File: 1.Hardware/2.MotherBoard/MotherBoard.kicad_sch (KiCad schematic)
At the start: 48 parts, among them J1 PWR, J2 MOTOR, SW1 SW_SPDT, U1 SCEP_CH32V3, U2 RT9013-33GB

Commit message: MotherBoard sch
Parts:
- added BZ1: Buzzer, ErBW_s:Buzzer_9*9P5, symbol Device:Buzzer
- added D7: 1N4148W, Diode_SMD:D_SMA, symbol Diode:1N4148W
- added J3: SWD, symbol Connector_Generic:Conn_02x04_Odd_Even
- added J4: WIRELESS, Connector_PinHeader_2.54mm:PinHeader_1x04_P2.54mm_Vertical, symbol Connector_Generic:Conn_01x04
- added J5: FLY_WHEEL, Connector_PinHeader_2.54mm:PinHeader_2x03_P2.54mm_Vertical, symbol Connector_Generic:Conn_02x03_Odd_Even
- added J6: MOTOR_BACK, Connector_PinHeader_2.54mm:PinHeader_2x03_P2.54mm_Vertical, symbol Connector_Generic:Conn_02x03_Odd_Even
- added J7: SERVO, Connector_PinHeader_2.54mm:PinHeader_1x03_P2.54mm_Vertical, symbol Connector_Generic:Conn_01x03
- added J8: MOTOR, ErBW_s:VCC_CONN, symbol Connector_Generic:Conn_01x02
- added J9: 9-Axis, Connector_PinHeader_2.54mm:PinHeader_1x04_P2.54mm_Vertical, symbol Connector_Generic:Conn_01x04
- added Q2: S8050, Package_TO_SOT_SMD:SOT-23, symbol Transistor_BJT:2N3055
- added R13, R14, R16, R18, R20: 5K1, Resistor_SMD:R_0603_1608Metric, symbol Device:R_Small
- added R15, R17, R19, R21: 10K, Resistor_SMD:R_0603_1608Metric, symbol Device:R_Small
- added U5: MT9V034, Connector_FFC-FPC:Hirose_FH12-18S-0.5SH_1x18-1MP_P0.50mm_Horizontal, symbol ErBW_s:MT9V034
- J2: footprint Connector_AMASS:AMASS_XT30U-M_1x02_P5.0mm_Vertical -> ErBW_s:VCC_CONN
- U3, U4: value ~ -> ME3116
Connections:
- net +3V3: now also BZ1.1 (-), J3.2 (Pin_2), U5.17 (VCC), U5.18 (VCC)
- net +5V: now also J4.4 (Pin_4), J9.1 (Pin_1)
- net +6V: now also J7.2 (Pin_2)
- net BATTERY: now also U1.64 (ADC_VABT)
- net CAM_D0: now also U5.8 (D0)
- net CAM_D1: now also U5.9 (D1)
- net CAM_D2: now also U5.10 (D2)
- net CAM_D3: now also U5.11 (D3)
- net CAM_D4: now also U5.12 (D4)
- net CAM_D5: now also U5.13 (D5)
- net CAM_D6: now also U5.14 (D6)
- net CAM_D7: now also U5.15 (D7)
- net CAM_HREF: now also U5.5 (HREF)
- net CAM_PLCK: now also U5.1 (PCLK)
- net CAM_RXD: now also U5.3 (TX)
- net CAM_TXD: now also U5.4 (RX)
- net CAM_VSYNC: now also U5.6 (VSYNC)
- net GND: now also J3.8 (Pin_8), J4.3 (Pin_3), J5.3 (Pin_3), J5.4 (Pin_4), J6.3 (Pin_3), J6.4 (Pin_4), J7.1 (Pin_1), J9.2 (Pin_2), Q2.2 (E), R13.2, R15.1, R17.1, R19.1, R21.1, U5.16 (GND), U5.2 (GND), U5.7 (GND), U5.MP (NC)
- net GNDPWR: now also J2.2 (Pin_2), J8.2 (Pin_2); no longer J2.1 (Pin_1)
- net MOTOR_PWR: now also J2.1 (Pin_1), J8.1 (Pin_1); no longer J2.2 (Pin_2)
- net MOTOR_DIR: now reaches U1., U1.10 (1DIR)
- net MOTOR_DIR: now also J6.1 (Pin_1)
- net SWCLK: now reaches U1.1 (SWCLK)
- net SWCLK: now also J3.6 (Pin_6)
- net MOTOR_PWM: now reaches U1.11 (1PWM)
- net MOTOR_PWM: now also J6.5 (Pin_5)
- net WHEEL_DIR: now reaches U1.12 (2DIR)
- net WHEEL_DIR: now also J5.1 (Pin_1)
- net WHEEL_PWM: now reaches U1.13 (2PWM)
- net WHEEL_PWM: now also J5.5 (Pin_5)
- net WHEEL_SPD_IN_3V3: now reaches U1.14 (ENC_2LSB)
- net WHEEL_SPD_IN_3V3: now also R16.1, R17.2
- net WHEEL_DIR_IN_3V3: now reaches U1.16 (ENC_2DIR)
- net WHEEL_DIR_IN_3V3: now also R14.1, R15.2
- net SWDIO: now reaches U1.2 (SWDIO)
- net SWDIO: now also J3.4 (Pin_4)
- net UART3_RX: now reaches U1.3 (UART3_RX)
- net UART3_RX: now also J3.1 (Pin_1)
- net UART7_RX: now reaches U1.35 (UART7_RX)
- net UART7_RX: now also J4.2 (Pin_2)
- net UART7_TX: now reaches U1.36 (UART7_TX)
- net UART7_TX: now also J4.1 (Pin_1)
- net UART3_TX: now reaches U1.4 (UART3_TX)
- net UART3_TX: now also J3.3 (Pin_3)
- net SERVO: now reaches U1.40 (PA15)
- net SERVO: now also D7.2 (A)
- net MOTOR_DIR_IN_3V3: now reaches U1.41 (ENC_1DIR)
- net MOTOR_DIR_IN_3V3: now also R18.1, R19.2
- net MOTOR_SPD_IN_3V3: now reaches U1.43 (ENC_1LSB)
- net MOTOR_SPD_IN_3V3: now also R20.1, R21.2
- net AUX_SCL: now reaches U1.48 (AUX_SCL)
- net AUX_SCL: now also J9.3 (Pin_3)
- net AUX_SDA: now reaches U1.49 (AUX_SDA)
- net AUX_SDA: now also J9.4 (Pin_4)
- net BUZZER: now reaches U1.50 (BUZZER)
- net BUZZER: now also Q2.1 (B), R13.1
- new net: BZ1.2 (+), Q2.3 (C)
- new net: D7.1 (K), J7.3 (Pin_3)
- new net MOTOR_DIR_IN: J6.2 (Pin_2), R18.2
- new net MOTOR_SPD_IN: J6.6 (Pin_6), R20.2
- new net WHEEL_DIR_IN: J5.2 (Pin_2), R14.2
- new net WHEEL_SPD_IN: J5.6 (Pin_6), R16.2
- no-connect marks 1 -> 3
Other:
- moved on the sheet: C1, C2, C3, D1, R1, U2

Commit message: 母板初步布局
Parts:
- removed D3, D6, D7: 1N4148W, Diode_SMD:D_SMA, symbol Diode:1N4148W
- removed J3: SWD, symbol Connector_Generic:Conn_02x04_Odd_Even
- added D1 (x2): 1N5819, ErBW_s:SOD-323, symbol Diode:1N5819WS
- added F?: 500mA, Fuse:Fuse_0603_1608Metric, symbol Device:Fuse_Small
- added J10: GPS, Connector_PinSocket_2.54mm:PinSocket_1x04_P2.54mm_Vertical, symbol Connector_Generic:Conn_01x04
- BZ1: footprint ErBW_s:Buzzer_9*9P5 -> ErBW_s:DET-402-G-1
- J4: footprint Connector_PinHeader_2.54mm:PinHeader_1x04_P2.54mm_Vertical -> Connector_PinSocket_2.54mm:PinSocket_1x04_P2.54mm_Vertical
- J5: renamed from J2; footprint ErBW_s:VCC_CONN -> Connector_AMASS:AMASS_XT30PW-F_1x02_P2.50mm_Horizontal
- J6: renamed from J5; footprint Connector_PinHeader_2.54mm:PinHeader_2x03_P2.54mm_Vertical -> Connector_PinHeader_2.54mm:PinHeader_2x03_P2.54mm_Horizontal
- J7: renamed from J8; footprint ErBW_s:VCC_CONN -> Connector_AMASS:AMASS_XT30PW-F_1x02_P2.50mm_Horizontal
- J8: renamed from J6; footprint Connector_PinHeader_2.54mm:PinHeader_2x03_P2.54mm_Vertical -> Connector_PinHeader_2.54mm:PinHeader_2x03_P2.54mm_Horizontal
- L1, L2: footprint (none) -> Inductor_SMD:L_Sunlord_SWPA4030S
- TP1: footprint TestPoint:TestPoint_Pad_D2.5mm -> TestPoint:TestPoint_Pad_D1.5mm
- TP2: renamed from TP3; footprint TestPoint:TestPoint_Pad_D2.5mm -> TestPoint:TestPoint_Pad_D1.5mm
- TP4: renamed from TP5; footprint TestPoint:TestPoint_Pad_D2.5mm -> TestPoint:TestPoint_Pad_1.5x1.5mm
- U4: renamed from U1; footprint (none) -> ErBW_s:SCEP_CH32V3
- renumbered C14 to C1, C2 to C10, C3 to C11, C5 to C12, C6 to C13, C8 to C14, C10 to C15, C15 to C16, C16 to C17, C4 to C2, C11 to C3, C9 to C4, C7 to C5, C13 to C6, C17 to C7, C12 to C8, C1 to C9, D4 to D1, D1 to D4, J9 to J1, J1 to J3, J7 to J9, Q2 to Q1, R2 to R1, R4 to R10, R1 to R11, R9 to R12, R14 to R13, R16 to R14, R10 to R15, R15 to R16, R11 to R18, R8 to R19, R6 to R2, R12 to R20, R13 to R21, R18 to R4, R20 to R5, R7 to R6, R19 to R7, R21 to R8, R5 to R9, TP2 to TP3, U4 to U1
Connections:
- net +5V: now also U4.37 (5V), U4.38 (5V), U4.39 (5V), J10.4 (Pin_4)
- net GND: now also U4.55 (GND), U4.56 (GND), U4.57 (GND), U4.58 (GND), J10.3 (Pin_3)
- net GNDPWR: now also J5.1 (Pin_1), J7.1 (Pin_1), D1.2 (A), D1.2 (A); no longer J5.2 (Pin_2), J7.2 (Pin_2)
- net MOTOR_PWR: now also J5.2 (Pin_2), J7.2 (Pin_2); no longer J5.1 (Pin_1), J7.1 (Pin_1)
- net SERVO: now also F?.1
- net at C12.2, C14.2, L2.1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: now also D1.1 (K)
- net at C1.2, C4.2, L1.1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: now also D1.1 (K)
- net at J9.3 (Pin_3): now also F?.2
- net UART8_RX: now reaches U4.33 (PE15)
- net UART8_RX: now also J10.2 (Pin_2)
- net UART8_TX: now reaches U4.34 (PE14)
- net UART8_TX: now also J10.1 (Pin_1)
- net SWCLK: no longer names the net of U4.1 (SWCLK)
- net SWDIO: no longer names the net of U4.2 (SWDIO)
- net UART3_RX: no longer names the net of U4.3 (UART3_RX)
- net UART3_TX: no longer names the net of U4.4 (UART3_TX)
- no-connect marks 3 -> 36
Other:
- note added: "CAM"
- note added: "MCU"
- note added: "PORTS"
- note added: "PROTECTION"
- moved on the sheet: BZ1, J1, J3, J4, J5, J6, J7, J8, J9, Q1, R13, R14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

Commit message: MotherBoard finished
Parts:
- C1, C10, C11, C12, C13, C14, C15, C16, C17, C3, C4, C5, C6, C7, C8, C9: footprint Capacitor_SMD:C_0603_1608Metric -> ErBW_s:C_0402
- D2, D4, D5: footprint LED_SMD:LED_0805_2012Metric -> LED_SMD:LED_0603_1608Metric
- L1, L2: footprint Inductor_SMD:L_Sunlord_SWPA4030S -> ErBW_s:L_NR201612
- R1, R10, R11, R12, R13, R14, R15, R16, R17, R18, R2, R20, R21, R3, R4, R5, R6, R7, R8, R9: footprint Resistor_SMD:R_0603_1608Metric -> ErBW_s:R_0402
- TP1, TP2: footprint TestPoint:TestPoint_Pad_D1.5mm -> TestPoint:TestPoint_Pad_D1.0mm
- TP4: footprint TestPoint:TestPoint_Pad_1.5x1.5mm -> TestPoint:TestPoint_Pad_1.0x1.0mm
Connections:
- net GND: now also C7.1, J5.1 (Pin_1), J7.1 (Pin_1), R6.2
- net GNDPWR: no longer C7.1, J5.1 (Pin_1), J7.1 (Pin_1), R6.2

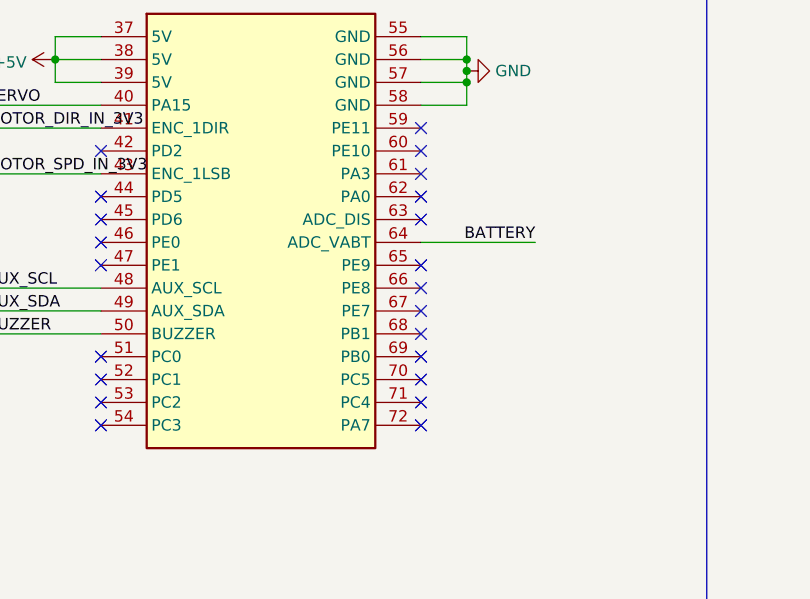
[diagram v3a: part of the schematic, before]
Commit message: new ips096 lib for ui usage
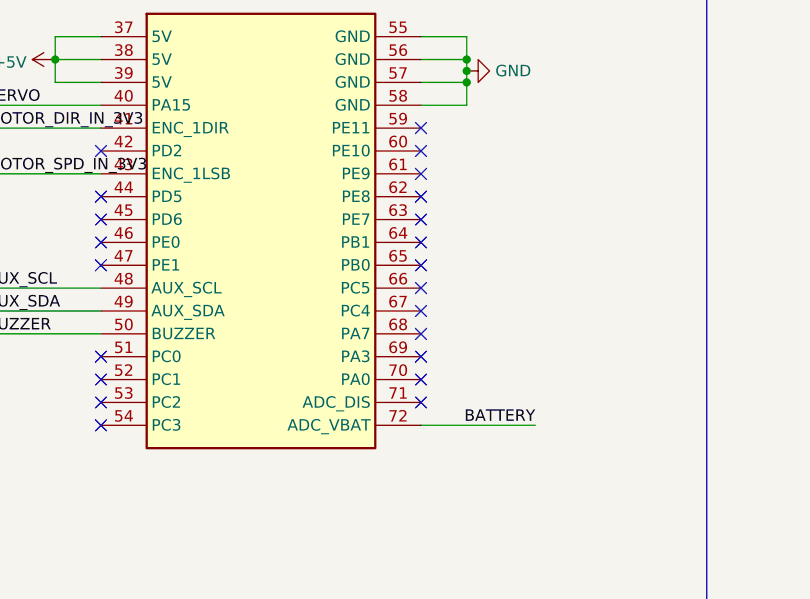
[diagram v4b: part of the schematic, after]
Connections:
- net BATTERY: now also U4.72 (ADC_VBAT); no longer U4.64 (ADC_VABT)
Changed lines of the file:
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@@
   (no_connect (at 152.4 168.91))
   (no_connect (at 116.84 168.91))
+  (no_connect (at 152.4 171.45))
   (no_connect (at 116.84 184.15))
   (no_connect (at 116.84 173.99))
@@
   (no_connect (at 46.99 148.59))
   (no_connect (at 46.99 191.77))
-  (no_connect (at 152.4 191.77))
   (no_connect (at 46.99 153.67))
+  (wire (pts (xy 152.4 191.77) (xy 165.1 191.77))
+    (stroke (width 0) (type default))
+  )
   (wire (pts (xy 137.16 40.64) (xy 137.16 41.91))
     (stroke (width 0) (type default))
@@
   )
   (wire (pts (xy 111.76 153.67) (xy 111.76 151.13))
-    (stroke (width 0) (type default))
-  )
-  (wire (pts (xy 152.4 171.45) (xy 165.1 171.45))
     (stroke (width 0) (type default))
   )
@@
     (effects (font (size 1.27 1.27)) (justify right bottom))
   )
-  (label "BATTERY" (at 165.1 171.45 180) (fields_autoplaced)
-    (effects (font (size 1.27 1.27)) (justify right bottom))
-  )
+  (label "BATTERY" (at 165.1 191.77 180) (fields_autoplaced)
+    (effects (font (size 1.27 1.27)) (justify right bottom))
+  )

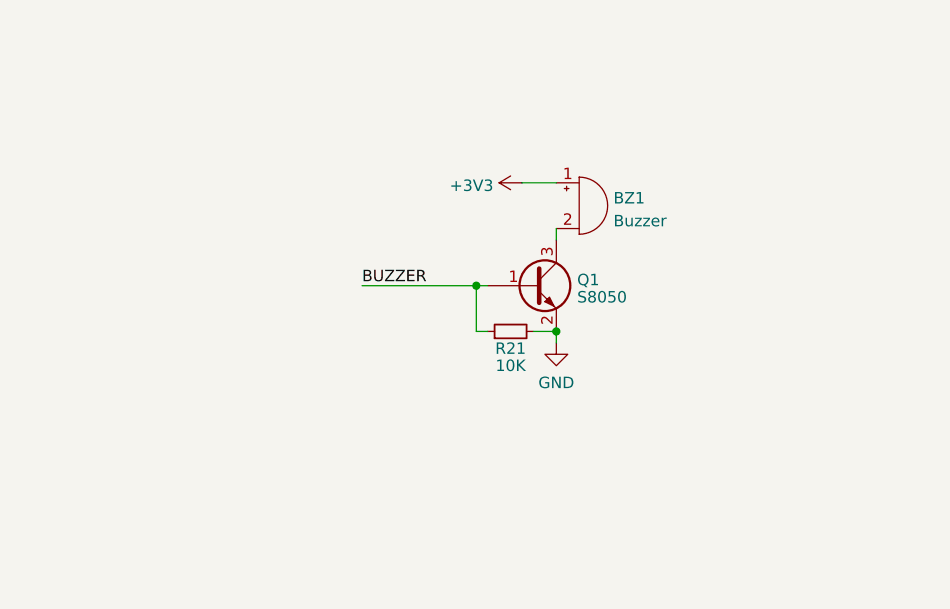
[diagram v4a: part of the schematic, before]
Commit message: MotherBoard v1.1 and AIO driver board sch
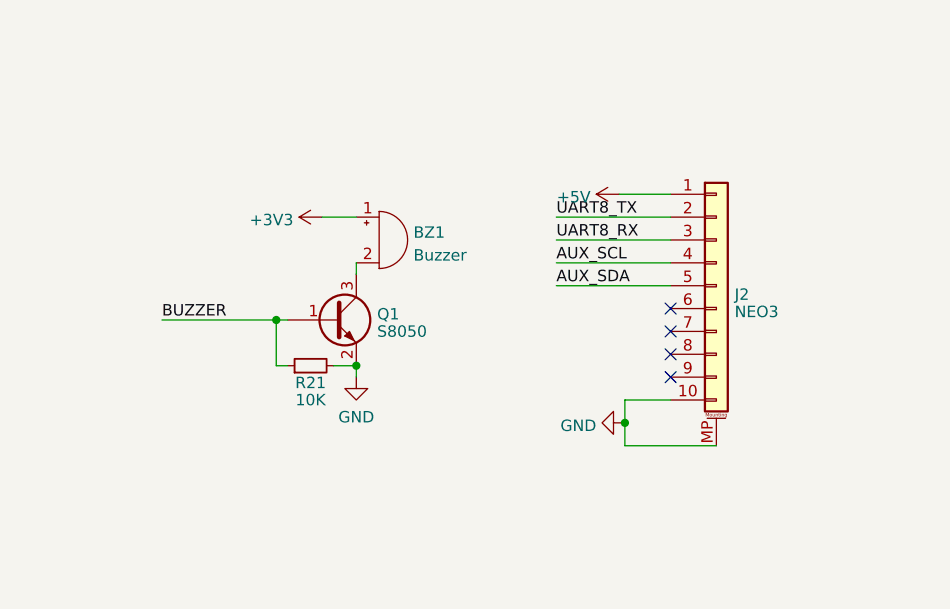
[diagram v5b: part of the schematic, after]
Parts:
- added J2: NEO3, Connector_JST:JST_GH_SM10B-GHS-TB_1x10-1MP_P1.25mm_Horizontal, symbol Connector_Generic_MountingPin:Conn_01x10_MountingPin
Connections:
- net +5V: now also J2.1 (Pin_1)
- net AUX_SCL: now also J2.4 (Pin_4)
- net AUX_SDA: now also J2.5 (Pin_5)
- net GND: now also J2.10 (Pin_10), J2.MP (MountPin)
- net UART8_RX: now also J2.3 (Pin_3)
- net UART8_TX: now also J2.2 (Pin_2)
- no-connect marks 36 -> 40
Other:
- moved on the sheet: BZ1, Q1, R21
